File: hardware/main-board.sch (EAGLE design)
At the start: 8 parts

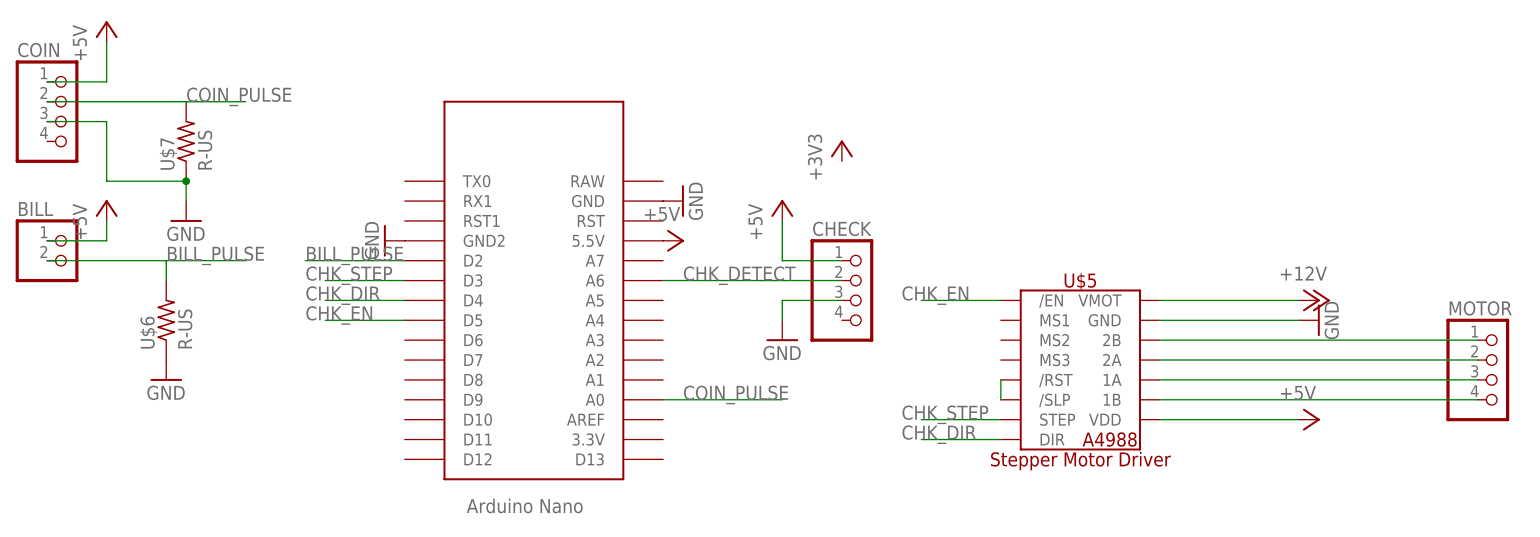
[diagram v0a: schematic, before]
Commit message: fix board layout - motor outputs corrected - pullup resistor corrected on coin acceptor
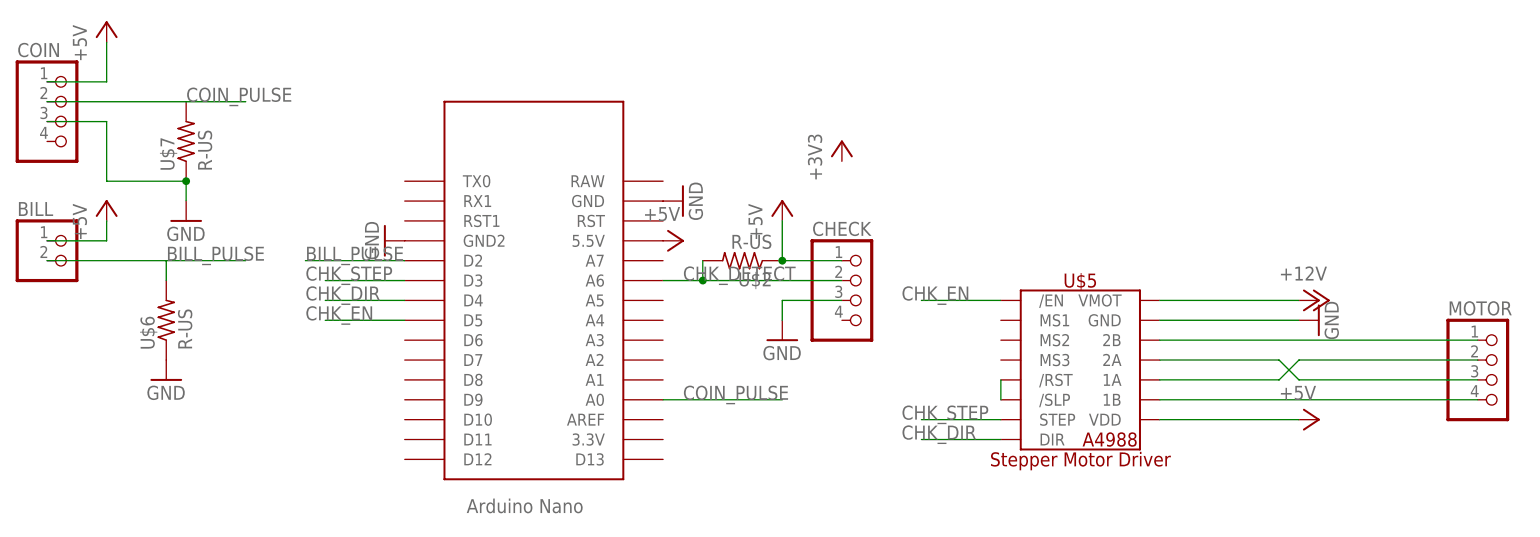
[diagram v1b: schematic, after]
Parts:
- added U$2: R-US, mcp:R-US
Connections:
- removed net N$5: MOTOR.2, U$5.2A
- removed net N$6: MOTOR.3, U$5.1A
- new net N$1: MOTOR.2, U$5.1A
- new net N$2: MOTOR.3, U$5.2A
- net +5V: now also U$2.1
- net CHK_DETECT: now also U$2.2
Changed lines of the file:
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@@
 <parts>
 <part name="U$1" library="Arduino-clone" deviceset="NANO" device=""/>
-<part name="U$2" library="Clean-Kong" deviceset="A4988" device=""/>
-<part name="U$3" library="Clean-Kong" deviceset="A4988" device=""/>
-<part name="U$4" library="Clean-Kong" deviceset="A4988" device=""/>
 <part name="U$5" library="IC" deviceset="A4988_STEP" device=""/>
 <part name="MOTOR" library="mcp" library_urn="urn:adsk.eagle:library:9418757" deviceset="PINHD-1X4" device="" package3d_urn="urn:adsk.eagle:package:22407/2"/>
@@
 <part name="U$7" library="mcp" library_urn="urn:adsk.eagle:library:9418757" deviceset="R-US" device="" package3d_urn="urn:adsk.eagle:package:23498/2"/>
 <part name="U$6" library="mcp" library_urn="urn:adsk.eagle:library:9418757" deviceset="R-US" device="" package3d_urn="urn:adsk.eagle:package:23498/2"/>
+<part name="U$2" library="mcp" library_urn="urn:adsk.eagle:library:9418757" deviceset="R-US" device="" package3d_urn="urn:adsk.eagle:package:23498/2"/>
 </parts>
 <sheets>
@@
 <attribute name="VALUE" x="-9.398" y="39.37" size="1.778" layer="96" rot="R90"/>
 </instance>
+<instance part="U$2" gate="G$1" x="60.96" y="50.8" smashed="yes" rot="R180">
+<attribute name="NAME" x="64.77" y="49.3014" size="1.778" layer="95" rot="R180"/>
+<attribute name="VALUE" x="64.77" y="54.102" size="1.778" layer="96" rot="R180"/>
+</instance>
 </instances>
 <busses>
@@
 <segment>
 <pinref part="U$1" gate="G$1" pin="A6"/>
-<wire x1="50.8" y1="48.26" x2="73.66" y2="48.26" width="0.1524" layer="91"/>
+<wire x1="50.8" y1="48.26" x2="55.88" y2="48.26" width="0.1524" layer="91"/>
 <label x="53.34" y="48.26" size="1.778" layer="95"/>
 <pinref part="CHECK" gate="A" pin="2"/>
+<pinref part="U$2" gate="G$1" pin="2"/>
+<wire x1="55.88" y1="48.26" x2="73.66" y2="48.26" width="0.1524" layer="91"/>
+<wire x1="55.88" y1="50.8" x2="55.88" y2="48.26" width="0.1524" layer="91"/>
+<junction x="55.88" y="48.26"/>
 </segment>
 </net>
@@
 <wire x1="114.3" y1="40.64" x2="154.94" y2="40.64" width="0.1524" layer="91"/>
 <pinref part="MOTOR" gate="A" pin="1"/>
-</segment>
-</net>
-<net name="N$5" class="0">
-<segment>
-<pinref part="U$5" gate="G$1" pin="2A"/>
-<wire x1="114.3" y1="38.1" x2="154.94" y2="38.1" width="0.1524" layer="91"/>
-<pinref part="MOTOR" gate="A" pin="2"/>
-</segment>
-</net>
-<net name="N$6" class="0">
-<segment>
-<pinref part="U$5" gate="G$1" pin="1A"/>
-<wire x1="114.3" y1="35.56" x2="154.94" y2="35.56" width="0.1524" layer="91"/>
-<pinref part="MOTOR" gate="A" pin="3"/>
 </segment>
 </net>
@@
 <pinref part="P+5" gate="1" pin="+5V"/>
 <wire x1="66.04" y1="50.8" x2="66.04" y2="55.88" width="0.1524" layer="91"/>
+<pinref part="U$2" gate="G$1" pin="1"/>
+<junction x="66.04" y="50.8"/>
 </segment>
 <segment>
@@
 </segment>
 </net>
+<net name="N$2" class="0">
+<segment>
+<wire x1="129.54" y1="38.1" x2="132.08" y2="35.56" width="0.1524" layer="91"/>
+<pinref part="U$5" gate="G$1" pin="2A"/>
+<wire x1="114.3" y1="38.1" x2="129.54" y2="38.1" width="0.1524" layer="91"/>
+<pinref part="MOTOR" gate="A" pin="3"/>
+<wire x1="132.08" y1="35.56" x2="154.94" y2="35.56" width="0.1524" layer="91"/>
+</segment>
+</net>
+<net name="N$1" class="0">
+<segment>
+<pinref part="U$5" gate="G$1" pin="1A"/>
+<wire x1="114.3" y1="35.56" x2="129.54" y2="35.56" width="0.1524" layer="91"/>
+<wire x1="129.54" y1="35.56" x2="132.08" y2="38.1" width="0.1524" layer="91"/>
+<pinref part="MOTOR" gate="A" pin="2"/>
+<wire x1="132.08" y1="38.1" x2="154.94" y2="38.1" width="0.1524" layer="91"/>
+</segment>
+</net>
